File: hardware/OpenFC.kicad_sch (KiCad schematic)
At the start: 0 parts

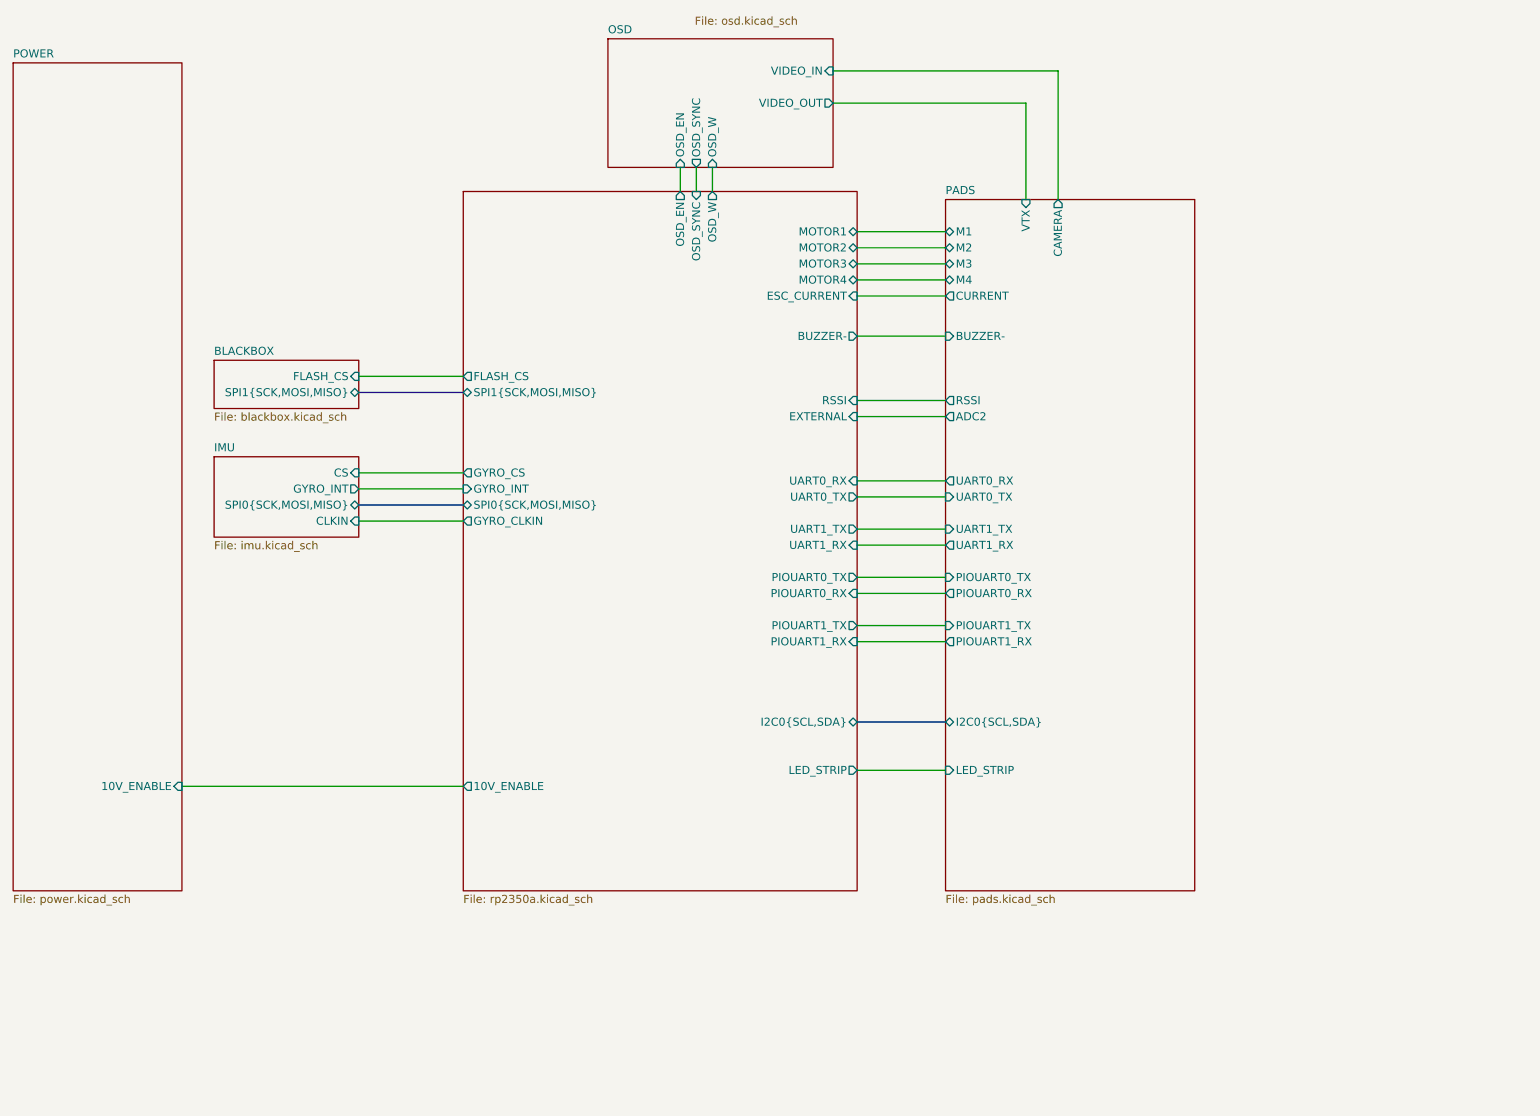
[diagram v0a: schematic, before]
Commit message: Rev 2: finalize schematic + PCB for fabrication
Rev 2 change list implemented; on-canvas design annotations added across all
sheets (root, rp2350a, power, imu, osd, blackbox, pads). Design frozen for ordering.

Co-Authored-By: Claude Opus 4.8 (1M context) <noreply@anthropic.com>
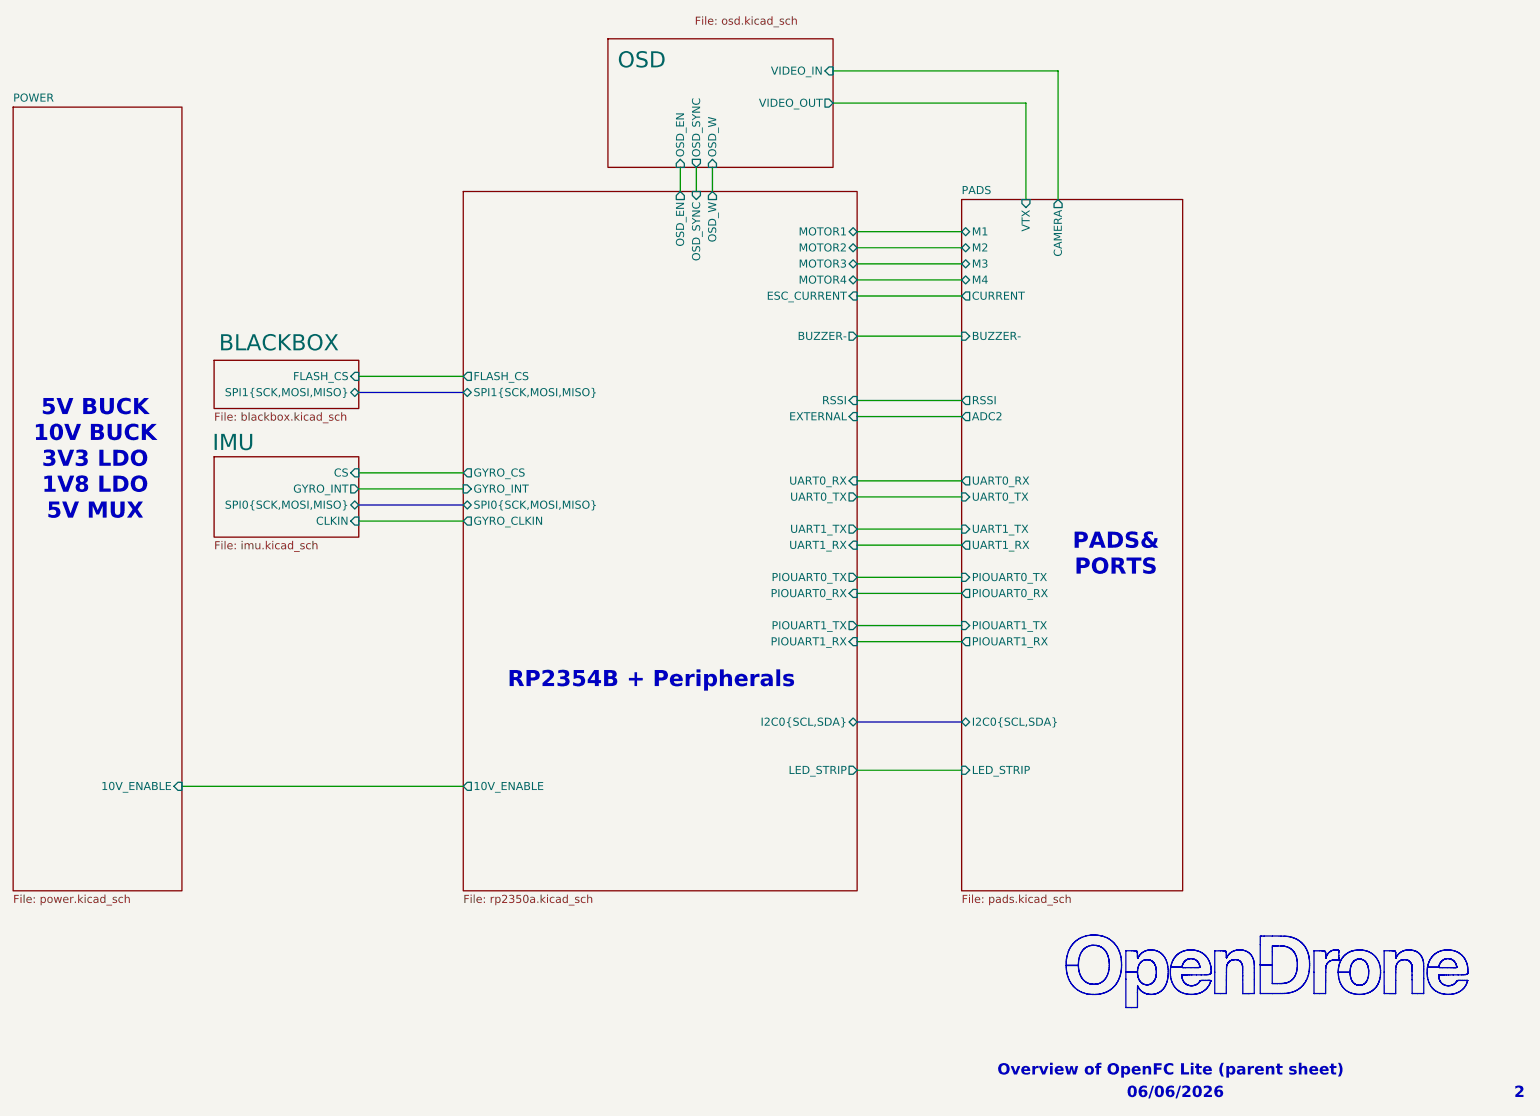
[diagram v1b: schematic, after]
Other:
- note added: "06/06/2026"
- note added: "2"
- note added: "5V BUCK 10V BUCK 3V3 LDO 1V8 LDO 5V MUX"
- note added: "Overview of OpenFC Lite (parent sheet)"
- note added: "PADS& PORTS"
- note added: "RP2354B + Peripherals"
